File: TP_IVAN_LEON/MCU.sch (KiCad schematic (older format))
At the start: 33 parts, among them P1 POWER IN, P3 CONN_01X06, P4 POWER_OUT, P5 ANALOG_IN, P6 DIN_5, U1 78L05, U4 LPC1769FBD100, U5 LD1117S12TR, X1 12MHZ, X2 32.768HZ

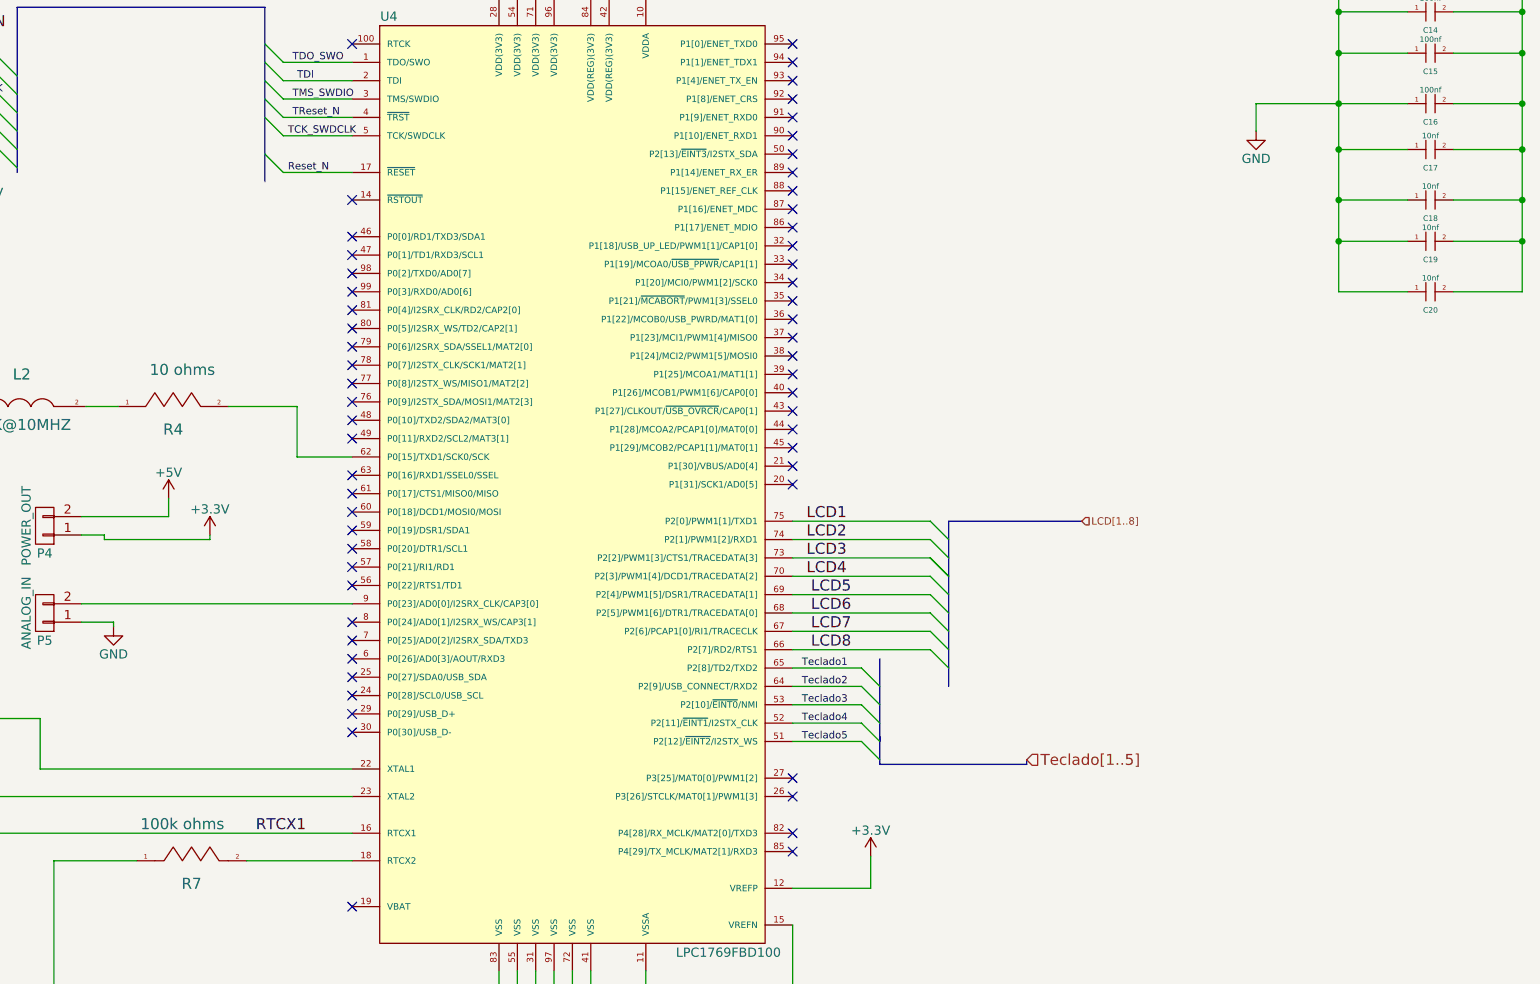
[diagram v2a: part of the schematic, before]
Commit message: Agrego Manf y Manf# en todos los componentes
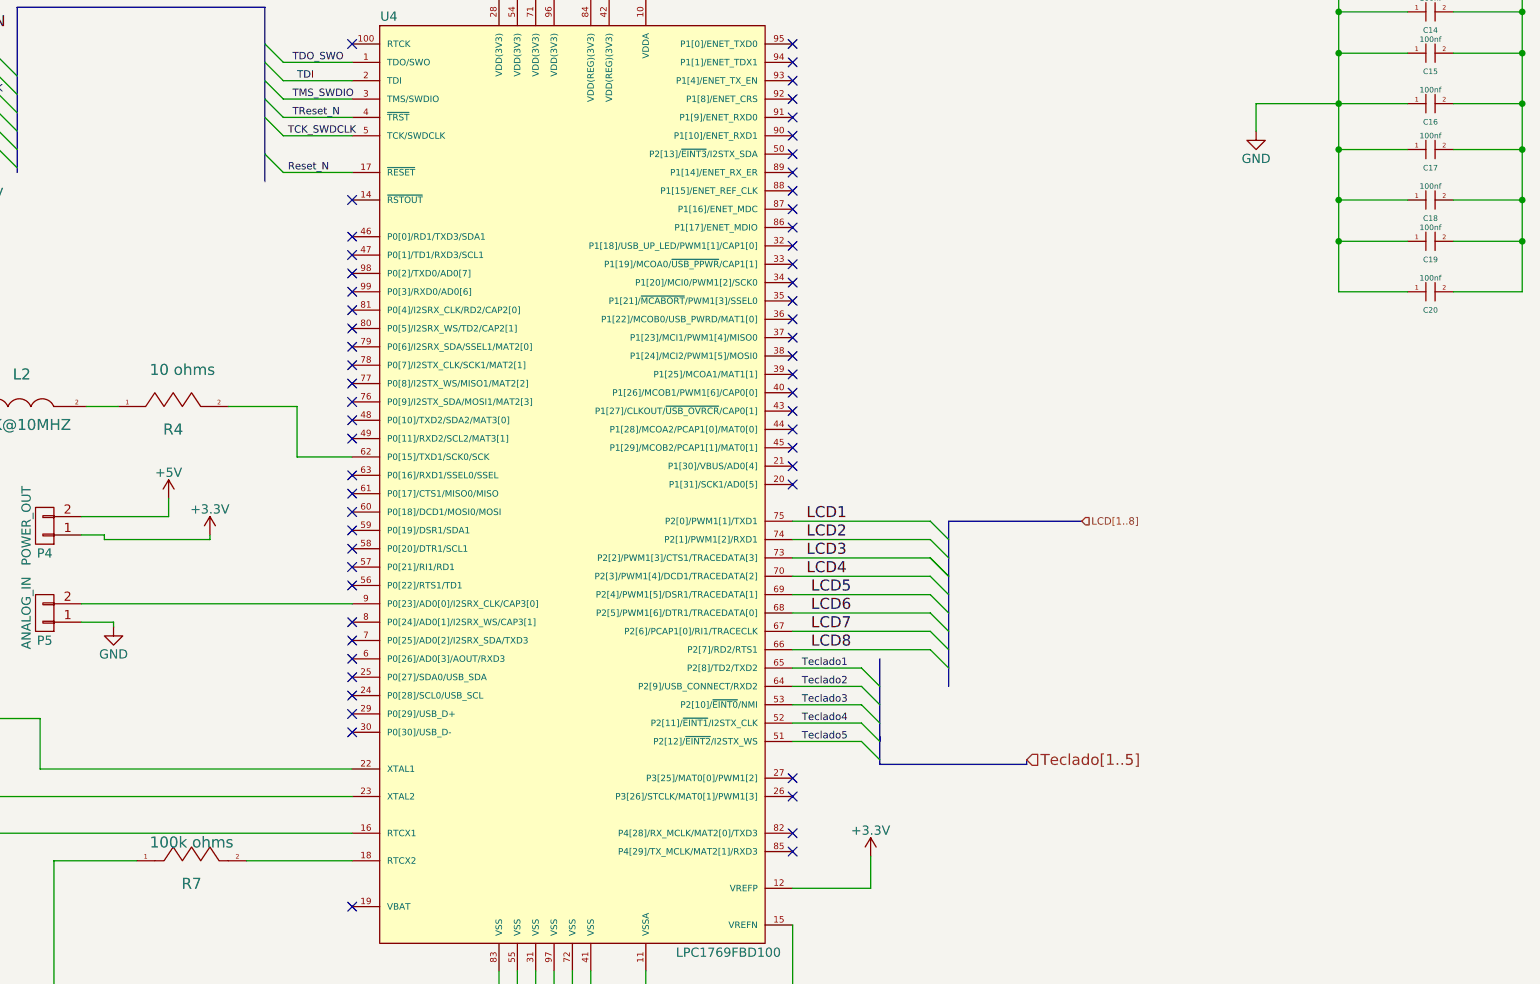
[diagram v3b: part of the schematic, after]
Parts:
- C10, C9: Manf (none) -> Kernet; Manf# (none) -> C1206C180D5GACTU
- C11, C12: Manf (none) -> AVX Corporation; Manf# (none) -> 12061A5R0CAT2A
- C13, C14, C15, C16: Manf (none) -> Samsung Electro-Mechanics America, Inc.; Manf# (none) -> CL21F104ZBCNNNC
- C17, C18, C19, C20: value 10nf -> 100nf; Digikey# 1276-2705-2-ND -> 1276-1007-1-ND; Manf (none) -> Samsung Electro-Mechanics America, Inc.; Manf# (none) -> CL21F104ZBCNNNC
- C6: Manf (none) -> Murata Electronics North America; Manf# (none) -> GRM21BR61C106KE15K
- C7, C8: Manf (none) -> Kemet; Manf# (none) -> C1206C105K4RACTU
- FB1, L2: Digikey# 732-10154-ND -> 732-6713-1-ND; Manf (none) -> Wurth Electronics Inc; Manf# (none) -> 782853112
- L3: Manf (none) -> Taiyo Yuden; Manf# (none) -> BK1608HS220-T
- P1, P4, P5: Manf (none) -> Molex, LLC; Manf# (none) -> 0530470210
- P3: Manf (none) -> Molex, LLC; Manf# (none) -> 0530470610
- P6: Manf (none) -> CUI Inc.; Manf# (none) -> SDS-50J
- R2: Manf (none) -> Yageo; Manf# (none) -> RC1206JR-0733RL
- R3: Manf (none) -> Vishay Dale; Manf# (none) -> CRCW06030000ZSTA
- R4: Manf (none) -> Yageo; Manf# (none) -> RC1206FR-0710RP
- R6: Manf (none) -> Yageo; Manf# (none) -> RC1206FR-071KP
- R7: Manf (none) -> Stackpole Electronics Inc.; Manf# (none) -> HVCB1206FKC100K
- U1: Manf (none) -> STMicroelectronics; Manf# (none) -> L78L05ACUTR
- U4: Manf (none) -> NXP Semiconductors; Manf# (none) -> LPC1769FBD100,551
- U5: Manf (none) -> STMicroelectronics; Manf# (none) -> LD1117S12TR
- X1: Manf (none) -> ECS Inc.; Manf# (none) -> ECS-120-20-4X
- X2: Manf (none) -> Citizen Finedevice Co Ltd; Manf# (none) -> CFS-20632768HZBB
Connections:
- net RTCX1: no longer names the net of C9.2, U4.16 (RTCX1), X2.2
